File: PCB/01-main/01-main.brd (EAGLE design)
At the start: 106 x 53 mm, 85 parts, among them IC1 NJU77551F, IC2 NJU77551F, J1 22057045, J10 22057045, J11 22057045, J12 22057045, J13 5267-4, J14 22057055, J8 22057045, J9 22057045, Q1 C1015, SW1 SK-12D11VG3, T1 BSS138, U1 CH340ESMD, U2 STM32F446RET6, U5 MAX485ESA+T, X1 Seeed Studio XIAO ESP32C3, X2 usb-c

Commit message: main配置完了
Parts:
- removed IC1, IC2: NJU77551F, burr-brown:SOT23-5
- removed J10, J11, J12, J9: 22057045, con-molex-5268:CON_22057045_MOL
- removed J13: 5267-4, con-molex-spox:5267-4
- removed R11: 180k, rcl:R0402
- removed R18, R19, R22, R23: 1k, rcl:R0402
- removed R20, R21, R24, R25: 330k, rcl:R0402
- removed R5, R6: 10k, rcl:R0402
- removed XT1: XT-30_L, XT-30:XT-30_L
- added C17, C19: 1µ, rcl:C0603
- added C18: 0.1µ, rcl:C0603
- added C20: 100μ, rcl:153CLV-0505
- added CN1: ML8, ML8:ML6L
- added D4: 1N4001, diode:SMA-DO214AC
- added JP1: (no value), pinhead-compact:1X02
- added JP2: (no value), pinhead-compact:1X05
- added REG3: REG-5V, #001-line:MYPARTS_D-PAK_TO252AA
- added SV1: (no value), con-ml:ML6L
- moved R13 218.2 mm to (31.0, 27.0), turned to 270 degrees
- moved R12 216.6 mm to (29.5, 27.0), turned to 270 degrees
- moved U4 216.4 mm to (37.0, 23.0)
- moved C15 203.0 mm to (11.0, 20.0)
- moved C4 186.6 mm to (8.00, 35.0), turned to 90 degrees
- moved T1 180.1 mm to (42.0, 33.0), turned to 270 degrees
- moved R31 179.4 mm to (5.00, 30.0), turned to 225 degrees
- moved SW1 178.1 mm to (4.00, 50.0)
- moved C2 175.1 mm to (0.00, 43.0), turned to 0 degrees
- moved C14 169.5 mm to (-15.2, 43.0), turned to 90 degrees
- moved R30 169.5 mm to (6.50, 39.0), turned to 135 degrees
- moved C12 169.5 mm to (23.0, 20.0)
- moved D3 169.1 mm to (30.0, 46.0)
- moved R10 166.8 mm to (-27.0, 46.0), turned to 0 degrees
- moved C16 165.5 mm to (4.50, 41.0), turned to 135 degrees
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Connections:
- removed net LCELL-L: IC1.1, R21.1
- removed net LCELL-R: IC2.1, R25.1
- removed net N$19: IC1.3, R18.1, R20.2
- removed net N$20: IC1.4, R19.1, R21.2
- removed net N$21: J10.3, R19.2
- removed net N$24: J10.4, R18.2
- removed net N$25: IC2.3, R22.1, R24.2
- removed net N$26: IC2.4, R23.1, R25.2
- removed net N$29: J12.4, R22.2
- removed net N$30: J12.3, R23.2
- new net LOADCELL-L: CN1.4, U2.10
- new net LOADCELL-R: CN1.3, U2.11
- new net MIRROR: CN1.8, U2.44
- new net VCC: C18.1, D4.A, J1.2, J8.2, REG3.3
- net +3V3: no longer IC1.5, IC2.5, J10.1, J12.1, R5.1, R6.1
- net +5V: now also SV1.2; no longer J1.2, J11.1, J8.2, R11.1
- net GND: now also C17.2, C18.2, C19.2, C20.-, CN1.1, J14.3, JP1.1, REG3.4, SV1.1; no longer IC1.2, IC2.2, J10.2, J11.2, J12.2, J13.P$4, R20.1, R24.1, XT1.2
- net LED-FLOOR: now also CN1.6; no longer J11.4
- net LED-UI: now also SV1.6; no longer J9.2
- net NRST: now also JP2.1; no longer J13.P$3
- net SERVO-SIG: now also CN1.7
- net SIG-FLOOR: now also CN1.5; no longer J11.3, R11.2
- net SW1: no longer J9.4, R5.2
- net SW2: no longer J9.3, R6.2
- net SWCLK: now also JP2.2; no longer J13.P$1
- net SWDIO: now also JP2.3; no longer J13.P$2
- net TOGGLE: now also SV1.5; no longer J9.1
- net UART1-RX: now also JP2.5
- net UART1-TX: now also JP2.4
- net UART3-RX: now also SV1.4; no longer X1.P$7
- net UART4-TX: now also SV1.3; no longer J14.3
- net VDD: now also C17.1, C19.1, C20.+, CN1.2, D4.K, REG3.1; no longer XT1.1
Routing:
- net GND: track 0.00 -> 306.3 mm, vias 0 -> 20
- net VDD: track 0.00 -> 113.6 mm, vias 0 -> 2
- net VCC: track 0.00 -> 95.9 mm
- net +5V: track 0.00 -> 69.9 mm, vias 0 -> 1
- net UART2-RX: track 0.00 -> 66.3 mm, vias 0 -> 1
- net UART2-TX: track 0.00 -> 66.1 mm, vias 0 -> 1
- net UART6-TX: track 0.00 -> 59.5 mm, vias 0 -> 2
- net UART6-RX: track 0.00 -> 57.1 mm, vias 0 -> 2
- net UART3-RX: track 0.00 -> 44.2 mm, vias 0 -> 1
- net SDA: track 0.00 -> 39.8 mm
- net TOGGLE: track 0.00 -> 39.8 mm, vias 0 -> 1
- net UART5-RX: track 0.00 -> 39.6 mm
- net UART4-TX: track 0.00 -> 38.7 mm, vias 0 -> 1
- net UART4-RX: track 0.00 -> 37.5 mm, vias 0 -> 1
- net LED-UI: track 0.00 -> 36.2 mm, vias 0 -> 1
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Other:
- outline, holes or cut-outs redrawn
- board text removed: "+"

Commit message: 微調整
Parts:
- moved LED1 18.0 mm to (-51.0, 6.00), turned to 90 degrees
- moved LED7 18.0 mm to (-51.0, 24.0), turned to 90 degrees
- moved LED2 12.0 mm to (-51.0, 9.00), turned to 90 degrees
- moved LED6 12.0 mm to (-51.0, 21.0), turned to 90 degrees
- moved LED3 6.00 mm to (-51.0, 12.0), turned to 90 degrees
- moved LED5 6.00 mm to (-51.0, 18.0), turned to 90 degrees
- moved C16 0.71 mm to (5.00, 41.5)
- moved R30 0.71 mm to (7.00, 39.5)
- turned LED4 to 90 degrees
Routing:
- net GND: track 306.3 -> 307.0 mm
- net NRST: track 3.17 -> 3.88 mm

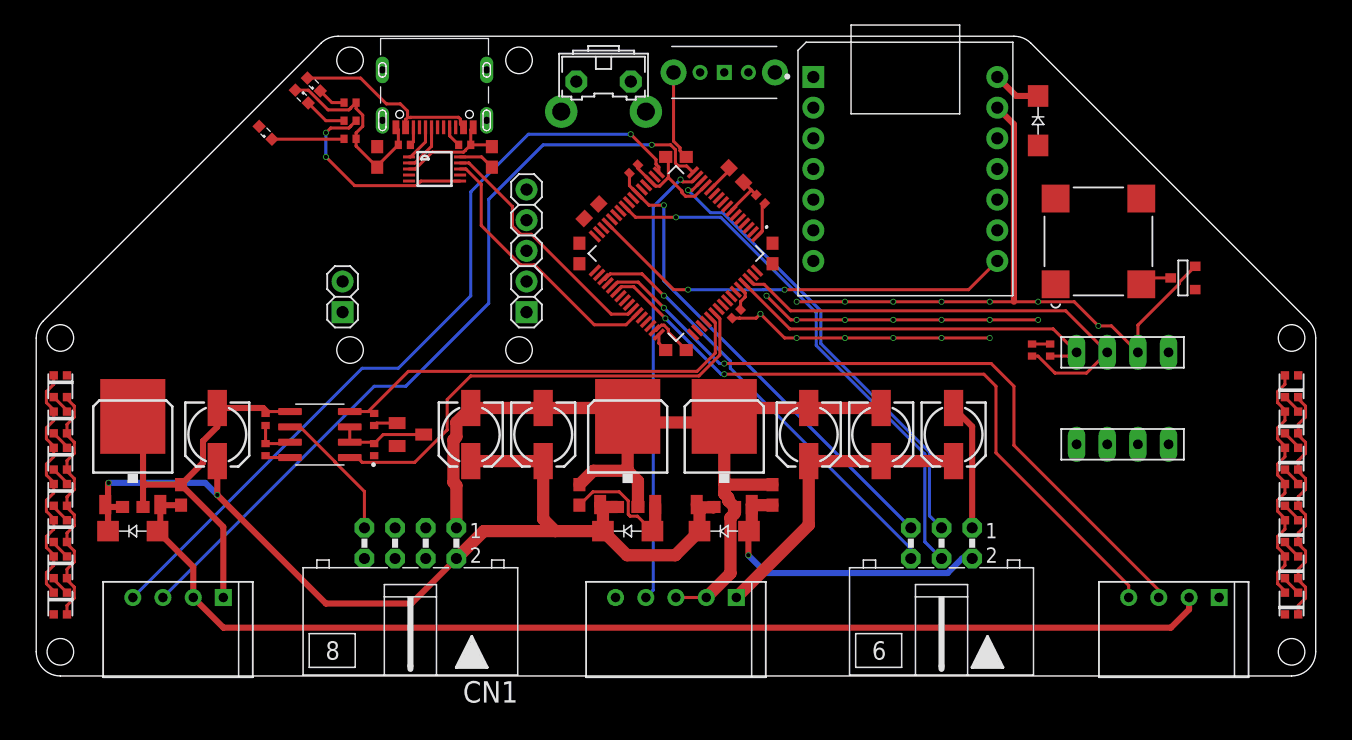
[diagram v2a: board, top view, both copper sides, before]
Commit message: メイン配線完了
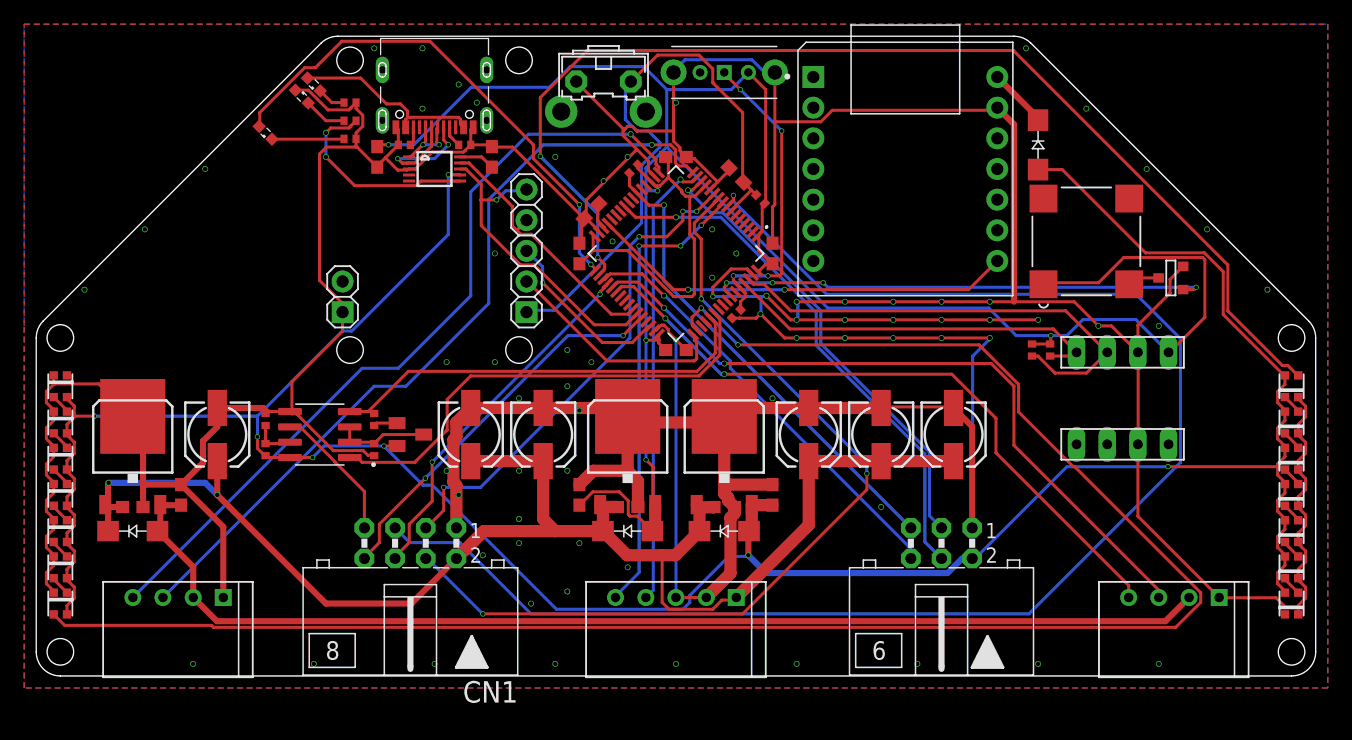
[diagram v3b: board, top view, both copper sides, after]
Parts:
- moved D3 2.00 mm to (30.0, 44.0)
- moved LS1 1.00 mm to (34.0, 36.0)
- moved T1 1.00 mm to (41.0, 33.0)
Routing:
- net GND: track 307.0 -> 526.1 mm, vias 20 -> 73
- net +3V3: track 26.7 -> 210.2 mm, vias 0 -> 5
- net +5V: track 69.9 -> 221.9 mm, vias 1 -> 7
- net LED-L: track 0.00 -> 151.9 mm, vias 0 -> 2
- net SIG-FLOOR: track 0.00 -> 126.8 mm, vias 0 -> 1
- net LED-R: track 0.00 -> 94.9 mm, vias 0 -> 2
- net LOADCELL-L: track 0.00 -> 73.6 mm, vias 0 -> 3
- net NRST: track 3.88 -> 49.3 mm
- net LED-WHITE: track 0.00 -> 42.4 mm, vias 0 -> 2
- net SPK: track 0.00 -> 41.7 mm, vias 0 -> 4
- net LOADCELL-R: track 0.00 -> 41.4 mm, vias 0 -> 4
- net LED-TOP: track 0.00 -> 38.4 mm, vias 0 -> 3
- net MIRROR: track 0.00 -> 32.2 mm, vias 0 -> 2
- net LED-FLOOR: track 0.00 -> 30.1 mm, vias 0 -> 2
- net BOOT0: track 2.15 -> 26.1 mm, vias 0 -> 4
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- added copper zone on layer 1, net GND
- added copper zone on layer 16, net GND

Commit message: 配置完了
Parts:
- moved D3 1.00 mm to (30.0, 45.0)
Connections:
- removed net SW1: U2.20
- removed net SW2: U2.21
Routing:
- net +3V3: track 210.2 -> 204.7 mm
- net UART1-TX: track 21.8 -> 20.2 mm
- net N$31: track 4.97 -> 4.44 mm
- net GND: vias 73 -> 79

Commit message: メイン配置おわ
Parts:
- removed C10, C12, C15: 100μ, rcl:153CLV-0505
- removed D3: 1N4001, diode:SMA-DO214AC
- removed X1: Seeed Studio XIAO ESP32C3, Seeeduino XIAO:XIAO-PINHEAD
- added U3: SUNA_LIB_M5STAMP_C3U_MATE, M5StampC3-pin:SUNA_LIB_M5STAMPC3UMATE
- moved LED1 18.0 mm to (-51.0, 24.0), turned to 270 degrees
- moved LED7 18.0 mm to (-51.0, 6.00), turned to 270 degrees
- moved LED2 12.0 mm to (-51.0, 21.0), turned to 270 degrees
- moved LED6 12.0 mm to (-51.0, 9.00), turned to 270 degrees
- moved R13 10.2 mm to (33.0, 17.0)
- moved R12 8.28 mm to (33.0, 19.5)
- moved LED3 6.00 mm to (-51.0, 18.0), turned to 270 degrees
- moved LED5 6.00 mm to (-51.0, 12.0), turned to 270 degrees
- moved U4 5.00 mm to (41.0, 20.0), turned to 270 degrees
- moved T1 4.47 mm to (45.0, 31.0)
- moved LS1 2.24 mm to (36.0, 35.0)
- turned LED4 to 270 degrees
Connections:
- removed net N$31: D3.K, X1.P$14
- net +5V: now also U3.5V1P, U3.5V2P; no longer D3.A
- net GND: now also U3.GND2P, U3.GND3P, U3.GND4P; no longer C10.-, C12.-, C15.-, X1.P$13
- net UART3-TX: now also U3.G20P; no longer X1.P$8
- net VDD: no longer C10.+, C12.+, C15.+
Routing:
- net GND: track 526.1 -> 217.4 mm, vias 79 -> 21
- net +3V3: track 204.7 -> 2.30 mm, vias 5 -> 0
- net +5V: track 222.3 -> 27.1 mm, vias 7 -> 0
- net LED-L: track 151.9 -> 0.00 mm, vias 2 -> 0
- net SIG-FLOOR: track 126.8 -> 0.00 mm, vias 1 -> 0
- net LED-R: track 94.9 -> 0.00 mm, vias 2 -> 0
- net VCC: track 94.9 -> 4.04 mm
- net LOADCELL-L: track 73.6 -> 0.00 mm, vias 3 -> 0
- net UART6-TX: track 59.5 -> 0.00 mm, vias 2 -> 0
- net UART6-RX: track 55.6 -> 0.00 mm, vias 2 -> 0
- net VDD: track 124.2 -> 73.9 mm, vias 2 -> 0
- net NRST: track 49.3 -> 0.00 mm
- net LED-WHITE: track 42.4 -> 0.00 mm, vias 2 -> 0
- net SPK: track 41.7 -> 0.00 mm, vias 4 -> 0
- net LOADCELL-R: track 41.4 -> 0.00 mm, vias 4 -> 0
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- removed copper zone on layer 1, net GND
- removed copper zone on layer 16, net GND

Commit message: ちびちび
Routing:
- net VCC: track 4.04 -> 95.1 mm
- net GND: track 217.4 -> 303.1 mm
- net VDD: track 73.9 -> 71.7 mm, vias 0 -> 2
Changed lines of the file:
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@@
 <wire x1="12" y1="23" x2="15" y2="20" width="0.254" layer="1"/>
 <wire x1="15" y1="20" x2="16" y2="20" width="0.254" layer="1"/>
+<wire x1="-34" y1="3" x2="42" y2="3" width="0.508" layer="16"/>
+<wire x1="42" y1="3" x2="45" y2="6" width="0.508" layer="16"/>
+<wire x1="45" y1="6" x2="45" y2="6.5" width="0.508" layer="16"/>
+<wire x1="-37.5" y1="6.5" x2="-34" y2="3" width="0.508" layer="16"/>
 <wire x1="51.55" y1="23.1" x2="46.016" y2="31.9398" width="0" layer="19" extent="1-1"/>
 <wire x1="45" y1="6.5" x2="51.55" y2="5.1" width="0" layer="19" extent="1-1"/>
@@
 <wire x1="-50.45" y1="23.1" x2="-50.45" y2="20.1" width="0" layer="19" extent="1-1"/>
 <wire x1="-27.62" y1="30.14" x2="-31.975" y2="21.905" width="0" layer="19" extent="1-1"/>
-<wire x1="-37.5" y1="6.5" x2="-41" y2="15.85" width="0" layer="19" extent="1-1"/>
 <wire x1="29.12" y1="42.08" x2="11.34" y2="39.54" width="0" layer="19" extent="1-1"/>
 </signal>
@@
 <wire x1="-47.05" y1="12" x2="-47.05" y2="13.97" width="1.016" layer="1"/>
 <wire x1="-45.85" y1="14" x2="-47" y2="14" width="1.016" layer="1"/>
-<wire x1="-38" y1="17.8" x2="-39.857" y2="15.943" width="1.016" layer="1"/>
-<wire x1="-41.786975" y1="10.515" x2="-44.113025" y2="10.515" width="1.016" layer="1"/>
-<wire x1="-45.598025" y1="12" x2="-47.05" y2="12" width="1.016" layer="1"/>
-<wire x1="-44.113025" y1="10.515" x2="-45.598025" y2="12" width="1.016" layer="1"/>
-<wire x1="-39.857" y1="15.943" x2="-39.857" y2="12.444975" width="1.016" layer="1"/>
-<wire x1="-39.857" y1="12.444975" x2="-41.786975" y2="10.515" width="1.016" layer="1"/>
+<wire x1="-38" y1="17.8" x2="-38.357" y2="17.443" width="1.016" layer="1"/>
+<wire x1="-38.357" y1="17.443" x2="-38.357" y2="16" width="1.016" layer="1"/>
+<wire x1="-47.28" y1="14.2" x2="-47.28" y2="15.72" width="0.508" layer="1"/>
+<wire x1="-47.28" y1="15.72" x2="-47" y2="16" width="0.508" layer="1"/>
+<via x="-47" y="16" extent="1-16" drill="0.35"/>
+<wire x1="-47" y1="16" x2="-38.357" y2="16" width="0.508" layer="16"/>
+<via x="-38.357" y="16" extent="1-16" drill="0.35"/>
 <wire x1="5" y1="6.5" x2="1.95" y2="12" width="0" layer="19" extent="1-1"/>
 <wire x1="-4.85" y1="14" x2="1.72" y2="14.2" width="0" layer="19" extent="1-1"/>
@@
 <contactref element="J8" pad="2"/>
 <contactref element="J1" pad="2"/>
-<wire x1="-42.72" y1="14.2" x2="-42.72" y2="12.23" width="1.016" layer="1"/>
+<wire x1="-42.72" y1="12.23" x2="-42.72" y2="14.2" width="1.016" layer="1"/>
 <wire x1="-42.72" y1="12.23" x2="-42.95" y2="12" width="1.016" layer="1"/>
 <wire x1="-42.72" y1="14.2" x2="-41.05" y2="14.2" width="1.016" layer="1"/>
 <wire x1="-41.05" y1="14.2" x2="-41" y2="14.15" width="1.016" layer="1"/>
-<wire x1="-39.9892" y1="6.5" x2="42.5108" y2="6.5" width="0" layer="19" extent="1-1"/>
-<wire x1="-42.95" y1="12" x2="-39.9892" y2="6.5" width="0" layer="19" extent="1-1"/>
+<wire x1="-42.95" y1="12" x2="-39.9892" y2="9.0392" width="0.508" layer="1"/>
+<wire x1="-39.9892" y1="9.0392" x2="-39.9892" y2="6.5" width="0.508" layer="1"/>
+<wire x1="-39.9892" y1="6.5" x2="-38.4892" y2="5" width="0.508" layer="1"/>
+<wire x1="-38.4892" y1="5" x2="42" y2="5" width="0.508" layer="1"/>
+<wire x1="42" y1="5" x2="42.5108" y2="5.5108" width="0.508" layer="1"/>
+<wire x1="42.5108" y1="5.5108" x2="42.5108" y2="6.5" width="0.508" layer="1"/>
 </signal>
 </signals>

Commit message: ねこ
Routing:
- net SDA: track 39.7 -> 40.4 mm
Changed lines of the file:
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@@
 <via x="26" y="18" extent="1-16" drill="0.35"/>
 <via x="21" y="18" extent="1-16" drill="0.35"/>
-<via x="21" y="20" extent="1-16" drill="0.35"/>
-<via x="26" y="20" extent="1-16" drill="0.35"/>
-<via x="31" y="20" extent="1-16" drill="0.35"/>
-<via x="31" y="16" extent="1-16" drill="0.35"/>
-<via x="26" y="16" extent="1-16" drill="0.35"/>
-<via x="21" y="16" extent="1-16" drill="0.35"/>
-<via x="14" y="17" extent="1-16" drill="0.35"/>
-<via x="10" y="21" extent="1-16" drill="0.35"/>
-<via x="5.5" y="25" extent="1-16" drill="0.35"/>
+<via x="21" y="19.2" extent="1-16" drill="0.35"/>
+<via x="26" y="19.2" extent="1-16" drill="0.35"/>
+<via x="31" y="19.2" extent="1-16" drill="0.35"/>
+<via x="31" y="16.7" extent="1-16" drill="0.35"/>
+<via x="26" y="16.7" extent="1-16" drill="0.35"/>
+<via x="21" y="16.7" extent="1-16" drill="0.35"/>
+<via x="14" y="17.5" extent="1-16" drill="0.35"/>
+<via x="10.2" y="21.3" extent="1-16" drill="0.35"/>
+<via x="6" y="25.5" extent="1-16" drill="0.35"/>
 <via x="5.5" y="29" extent="1-16" drill="0.35"/>
-<via x="15" y="16" extent="1-16" drill="0.35"/>
-<via x="16" y="20" extent="1-16" drill="0.35"/>
-<via x="12" y="23" extent="1-16" drill="0.35"/>
+<via x="15" y="16.7" extent="1-16" drill="0.35"/>
+<via x="16" y="19.2" extent="1-16" drill="0.35"/>
+<via x="11.8" y="22.8" extent="1-16" drill="0.35"/>
 <via x="9" y="26" extent="1-16" drill="0.35"/>
 <wire x1="-3.15" y1="14" x2="-3.15" y2="15.15" width="1.016" layer="1"/>
@@
 <wire x1="21" y1="18" x2="26" y2="18" width="0.254" layer="1"/>
 <wire x1="26" y1="18" x2="31" y2="18" width="0.254" layer="1"/>
-<wire x1="31" y1="20" x2="26" y2="20" width="0.254" layer="1"/>
-<wire x1="26" y1="20" x2="21" y2="20" width="0.254" layer="1"/>
-<wire x1="21" y1="20" x2="16" y2="20" width="0.254" layer="1"/>
-<wire x1="14" y1="17" x2="15" y2="16" width="0.254" layer="1"/>
-<wire x1="15" y1="16" x2="21" y2="16" width="0.254" layer="1"/>
-<wire x1="21" y1="16" x2="26" y2="16" width="0.254" layer="1"/>
-<wire x1="31" y1="16" x2="26" y2="16" width="0.254" layer="1"/>
-<wire x1="14" y1="17" x2="10" y2="21" width="0.254" layer="1"/>
-<wire x1="10" y1="21" x2="6" y2="25" width="0.254" layer="1"/>
-<wire x1="6" y1="25" x2="5.5" y2="25" width="0.254" layer="1"/>
-<wire x1="9" y1="26" x2="12" y2="23" width="0.254" layer="1"/>
-<wire x1="12" y1="23" x2="15" y2="20" width="0.254" layer="1"/>
-<wire x1="15" y1="20" x2="16" y2="20" width="0.254" layer="1"/>
+<wire x1="31" y1="19.2" x2="26" y2="19.2" width="0.254" layer="1"/>
+<wire x1="26" y1="19.2" x2="21" y2="19.2" width="0.254" layer="1"/>
+<wire x1="21" y1="19.2" x2="16" y2="19.2" width="0.254" layer="1"/>
+<wire x1="14" y1="17.5" x2="14.8" y2="16.7" width="0.254" layer="1"/>
+<wire x1="15" y1="16.7" x2="14.8" y2="16.7" width="0.254" layer="1"/>
+<wire x1="21" y1="16.7" x2="15" y2="16.7" width="0.254" layer="1"/>
+<wire x1="26" y1="16.7" x2="21" y2="16.7" width="0.254" layer="1"/>
+<wire x1="31" y1="16.7" x2="26" y2="16.7" width="0.254" layer="1"/>
+<wire x1="14" y1="17.5" x2="10.2" y2="21.3" width="0.254" layer="1"/>
+<wire x1="10.2" y1="21.3" x2="6" y2="25.5" width="0.254" layer="1"/>
+<wire x1="11.8" y1="22.8" x2="9" y2="25.6" width="0.254" layer="1"/>
+<wire x1="9" y1="26" x2="9" y2="25.6" width="0.254" layer="1"/>
+<wire x1="11.8" y1="22.8" x2="15.4" y2="19.2" width="0.254" layer="1"/>
+<wire x1="15.4" y1="19.2" x2="16" y2="19.2" width="0.254" layer="1"/>
 <wire x1="-34" y1="3" x2="42" y2="3" width="0.508" layer="16"/>
 <wire x1="42" y1="3" x2="45" y2="6" width="0.508" layer="16"/>
@@
 <wire x1="45" y1="6.5" x2="51.55" y2="5.1" width="0" layer="19" extent="1-1"/>
 <wire x1="44.81" y1="21.27" x2="51.55" y2="20.1" width="0" layer="19" extent="1-1"/>
-<wire x1="31" y1="20" x2="37.19" y2="21.27" width="0" layer="19" extent="1-1"/>
-<wire x1="11" y1="22" x2="12" y2="23" width="0" layer="19" extent="1-1"/>
-<wire x1="14" y1="17" x2="15" y2="18" width="0" layer="19" extent="1-1"/>
+<wire x1="31" y1="19.2" x2="37.19" y2="21.27" width="0" layer="19" extent="1-1"/>
+<wire x1="11" y1="22" x2="11.8" y2="22.8" width="0" layer="19" extent="1-1"/>
+<wire x1="14.8" y1="16.7" x2="15" y2="18" width="0" layer="19" extent="1-1"/>
 <wire x1="5.5" y1="29" x2="7" y2="26" width="0" layer="19" extent="1-1"/>
 <wire x1="4.64644375" y1="29.64644375" x2="5.5" y2="29" width="0" layer="19" extent="1-1"/>
@@
 <wire x1="6.363959375" y1="33.23223125" x2="7" y2="30" width="0" layer="19" extent="1-1"/>
 <wire x1="8" y1="35.85" x2="6.363959375" y2="33.23223125" width="0" layer="19" extent="1-1"/>
-<wire x1="4" y1="21.5" x2="5.5" y2="25" width="0" layer="19" extent="1-1"/>
-<wire x1="24.54" y1="12.27" x2="26" y2="16" width="0" layer="19" extent="1-1"/>
+<wire x1="4" y1="21.5" x2="6" y2="25.5" width="0" layer="19" extent="1-1"/>
+<wire x1="24.54" y1="12.27" x2="26" y2="16.7" width="0" layer="19" extent="1-1"/>
 <wire x1="0.85" y1="27" x2="4.64644375" y2="29.64644375" width="0" layer="19" extent="1-1"/>
 <wire x1="-1.767765625" y1="28.6360375" x2="0.85" y2="27" width="0" layer="19" extent="1-1"/>
 <wire x1="11.34" y1="39.54" x2="8" y2="35.85" width="0" layer="19" extent="1-1"/>
-<wire x1="8" y1="15.85" x2="10" y2="21" width="0" layer="19" extent="1-1"/>
+<wire x1="8" y1="15.85" x2="10.2" y2="21.3" width="0" layer="19" extent="1-1"/>
 <wire x1="-0.0038" y1="6.5" x2="2.5108" y2="6.5" width="0" layer="19" extent="1-1"/>
 <wire x1="2.828425" y1="40.3033" x2="8" y2="35.85" width="0" layer="19" extent="1-1"/>
@@
 <wire x1="33.27" y1="18.73" x2="37.19" y2="18.73" width="0.254" layer="1"/>
 <wire x1="8" y1="30.889084375" x2="6.01040625" y2="32.878678125" width="0.254" layer="1"/>
-<wire x1="33" y1="19" x2="15.2855375" y2="19" width="0.254" layer="1"/>
-<wire x1="15.2855375" y1="19" x2="8" y2="26.2855375" width="0.254" layer="1"/>
-<wire x1="8" y1="26.2855375" x2="8" y2="30.889084375" width="0.254" layer="1"/>
+<wire x1="33" y1="19" x2="32.6" y2="18.6" width="0.254" layer="1"/>
+<wire x1="32.6" y1="18.6" x2="15.1855375" y2="18.6" width="0.254" layer="1"/>
+<wire x1="15.1855375" y1="18.6" x2="8" y2="25.7855375" width="0.254" layer="1"/>
+<wire x1="8" y1="25.7855375" x2="8" y2="30.889084375" width="0.254" layer="1"/>
 </signal>
 <signal name="SCL">
@@
 <wire x1="36.88" y1="16.5" x2="33" y2="16.5" width="0.254" layer="1"/>
 <wire x1="33" y1="16.5" x2="32.5" y2="16.5" width="0.254" layer="1"/>
-<wire x1="32.5" y1="16.5" x2="32" y2="17" width="0.254" layer="1"/>
+<wire x1="32.5" y1="16.5" x2="31.6" y2="17.4" width="0.254" layer="1"/>
 <wire x1="6.369" y1="31.812978125" x2="5.656853125" y2="32.525125" width="0.254" layer="1"/>
-<wire x1="32" y1="17" x2="15.2855375" y2="17" width="0.254" layer="1"/>
-<wire x1="15.2855375" y1="17" x2="6.369" y2="25.9165375" width="0.254" layer="1"/>
+<wire x1="31.6" y1="17.4" x2="14.8855375" y2="17.4" width="0.254" layer="1"/>
+<wire x1="14.8855375" y1="17.4" x2="6.369" y2="25.9165375" width="0.254" layer="1"/>
 <wire x1="6.369" y1="25.9165375" x2="6.369" y2="31.812978125" width="0.254" layer="1"/>
 </signal>

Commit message: wet cat
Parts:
- moved T1 77.2 mm to (-32.0, 26.0), turned to 180 degrees
- moved LS1 72.0 mm to (-36.0, 33.0)
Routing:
- net UART5-RX: track 0.00 -> 38.9 mm
- net UART5-TX: track 0.00 -> 34.8 mm
- net GND: track 303.1 -> 322.7 mm
- net !RE: track 0.00 -> 7.75 mm
- net N$27: track 0.00 -> 1.98 mm
- net VDD: track 71.7 -> 73.3 mm
